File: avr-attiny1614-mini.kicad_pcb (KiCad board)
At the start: 2 copper layers, 0 parts

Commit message: Layout exploring
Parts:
- added C1: 100nF, local_footprints:0805_HS, F.Cu at (140.3, 138.4)
- added D1: D_Schottky, local_footprints:1206_Diode_HS, B.Cu at (149.9, 139.7)
- added J1: Conn_01x05, local_footprints:Pin_Header_Straight_1x05_Pitch2.54mm, F.Cu at (134.6, 144.8)
- added J10: UPDI, local_footprints:Pin_Header_Straight_1x01_Pitch2.54mm, F.Cu at (137.2, 134.6)
- added J2: Conn_01x06, local_footprints:Pin_Header_Straight_1x06_Pitch2.54mm, F.Cu at (139.7, 132.1)
- added J3: BAT_JST_PH, Connectors_JST:JST_PH_S2B-PH-K_02x2.00mm_Angled, F.Cu at (127.5, 142.2)
- added J4: GND, local_footprints:Pin_Header_Straight_1x01_Pitch2.54mm, F.Cu at (137.2, 132.1)
- added J5: GND, local_footprints:Pin_Header_Straight_1x01_Pitch2.54mm, F.Cu at (149.9, 144.8)
- added J6: VOUT1, local_footprints:Pin_Header_Straight_1x01_Pitch2.54mm, F.Cu at (152.4, 144.8)
- added J7: EXT_VIN, local_footprints:Pin_Header_Straight_1x01_Pitch2.54mm, F.Cu at (152.4, 135.9)
- added J8: EXT_LOAD+, local_footprints:Pin_Header_Straight_1x01_Pitch2.54mm, F.Cu at (152.4, 138.4)
- added J9: EXT_LOAD-, local_footprints:Pin_Header_Straight_1x01_Pitch2.54mm, F.Cu at (152.4, 141.0)
- added Q1: DMP2035U, local_footprints:SOT-23_HS, F.Cu at (130.8, 118.1)
- added Q2: NTR3C21NZ, local_footprints:SOT-23_HS, F.Cu at (156.2, 118.1)
- added R1: 3.3k, local_footprints:0805_HS, F.Cu at (137.2, 137.2)
- added R3: 100k, local_footprints:0805_HS, F.Cu at (135.9, 116.8)
- added R4: 100, local_footprints:1206_HS, F.Cu at (135.9, 119.4)
- added R5: 10k, local_footprints:0805_HS, F.Cu at (156.2, 125.7)
- added R6: 10k, local_footprints:0805_HS, F.Cu at (158.8, 125.7)
- added R7: 100, local_footprints:1206_HS, F.Cu at (130.8, 134.6)
- added R8: 1k, local_footprints:0805_HS, F.Cu at (151.1, 116.8)
- added R9: 100k, local_footprints:0805_HS, F.Cu at (151.1, 119.4)
- added SW1: SW_SPST, Buttons_Switches_THT:SW_PUSH_6mm, F.Cu at (133.3, 132.1)
- added U1: attiny1614, local_footprints:SOIC-14_3.9x8.7mm_Pitch1.27mm_HS, F.Cu at (146.1, 138.4)

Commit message: Approx placement for 1.2in x 0.6in board.
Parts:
- added J11: GND, local_footprints:Pin_Header_Straight_1x01_Pitch2.54mm, F.Cu at (127.0, 132.1)
- D1: moved to F.Cu
- Q1, R3, R4, R5, R6, R7: moved to B.Cu
- moved Q2 33.1 mm to (129.5, 137.7)
- moved R8 32.4 mm to (126.4, 137.8), turned to 90 degrees
- moved R9 32.4 mm to (124.5, 137.8), turned to 90 degrees
- moved J7 28.2 mm to (124.5, 132.1), turned to 90 degrees
- moved J8 23.7 mm to (129.5, 132.1), turned to 90 degrees
- moved J9 22.2 mm to (132.1, 132.1), turned to 90 degrees
- moved Q1 21.1 mm to (129.5, 139.2), turned to 0 degrees
- moved D1 20.9 mm to (129.5, 134.6), turned to 0 degrees
- moved R4 20.5 mm to (125.7, 137.2), turned to 270 degrees
- moved J6 20.3 mm to (132.1, 144.8)
- moved R3 19.5 mm to (129.4, 135.3)
- moved J4 13.0 mm to (134.6, 144.8)
- moved R5 11.8 mm to (149.9, 135.6)
- moved R6 11.8 mm to (152.4, 135.6), turned to 90 degrees
- moved R7 7.50 mm to (137.7, 137.7), turned to 90 degrees
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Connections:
- net Net-(D1-Pad1) renamed /EXT_VIN_LOAD+
- net Net-(D1-Pad2) renamed /EXT_LOAD-
- net Net-(J6-Pad1) renamed /VOUT1

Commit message: Routing part 1
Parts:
- removed the U1 at (148.6, 138.4)
- added U1 (x2): attiny1614, local_footprints:SOIC-14_3.9x8.7mm_Pitch1.27mm_HS, F.Cu at (148.6, 138.4)
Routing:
- net VIN: track 0.00 -> 20.5 mm, vias 0 -> 2
- net /~RESET: track 0.00 -> 18.9 mm, vias 0 -> 2
- net Net-(J1-Pad2): track 0.00 -> 8.36 mm
- net Net-(J1-Pad3): track 0.00 -> 8.20 mm
- net UPDI: track 0.00 -> 7.65 mm
- net /SCL: track 0.00 -> 6.84 mm
- net /SCK: track 0.00 -> 6.76 mm
- net Net-(R7-Pad1): track 0.00 -> 6.50 mm
- net /SDA: track 0.00 -> 6.34 mm
- net /RX: track 0.00 -> 6.33 mm
- net /TX: track 0.00 -> 5.38 mm
- net /MISO: track 0.00 -> 5.38 mm
- net GND: track 0.00 -> 5.38 mm
- net /MOSI: track 0.00 -> 4.43 mm

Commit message: Complete routing; Draft.
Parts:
- removed the U1 at (148.6, 138.4) (x2)
- added U1 (x2): attiny1614, local_footprints:SOIC-14_3.9x8.7mm_Pitch1.27mm_HS, F.Cu at (148.6, 138.4)
- moved J11 2.54 mm to (124.5, 132.1)
- moved J7 2.54 mm to (127.0, 132.1)
- moved R7 0.32 mm to (137.4, 137.7)
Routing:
- net GND: track 5.38 -> 39.2 mm, vias 0 -> 5
- net VEXT-EN: track 0.00 -> 28.6 mm, vias 0 -> 4
- net VOUT1-~EN: track 0.00 -> 24.9 mm, vias 0 -> 3
- net VIN: track 20.5 -> 43.4 mm, vias 2 -> 3
- net /VOUT1: track 0.00 -> 7.38 mm, vias 0 -> 2
- net /EXT_LOAD-: track 0.00 -> 7.15 mm
- net /EXT_VIN_LOAD+: track 0.00 -> 6.21 mm
- net Net-(Q1-Pad1): track 0.00 -> 4.93 mm, vias 0 -> 2
- net Net-(R7-Pad1): track 6.50 -> 9.70 mm
- net Net-(Q2-Pad1): track 0.00 -> 2.01 mm
- added copper zone on B.Cu, net GND
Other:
- board outline added: 30.5 x 15.2 mm

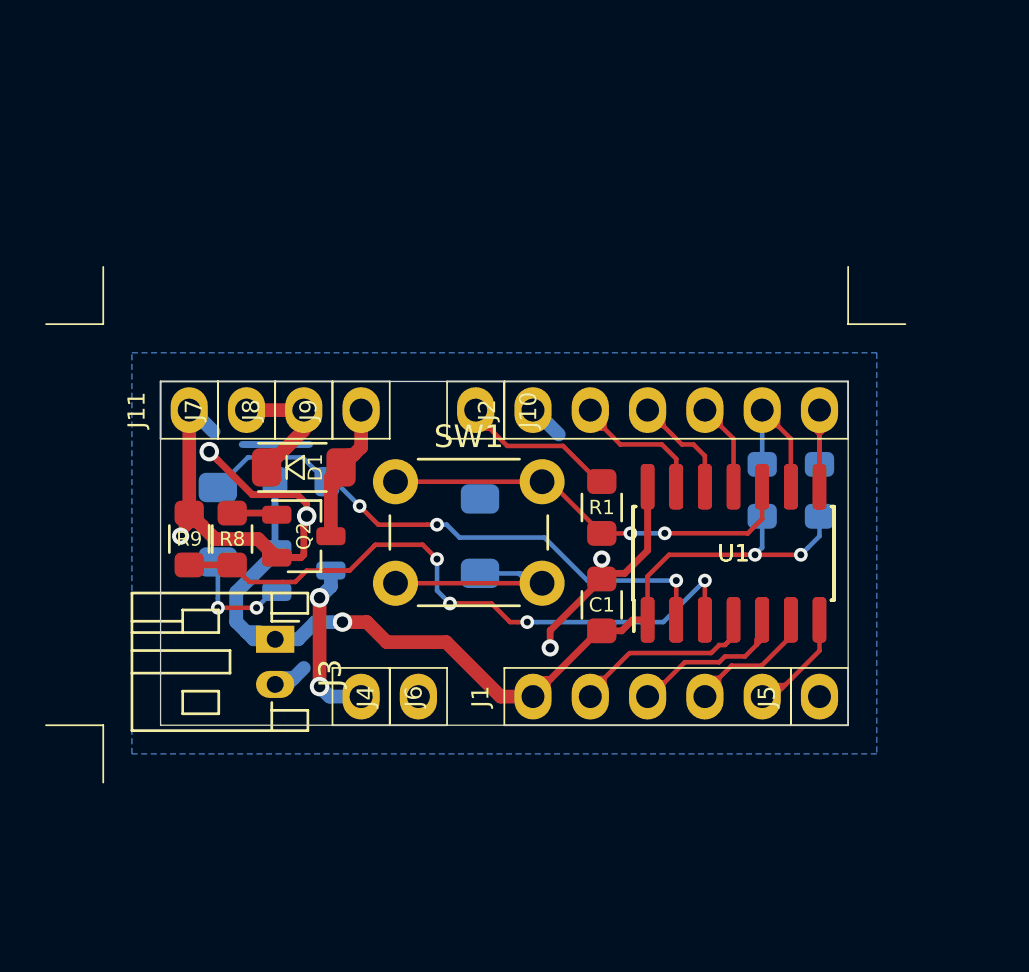
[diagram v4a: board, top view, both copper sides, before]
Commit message: Finished 1.2in x 0.6in layout
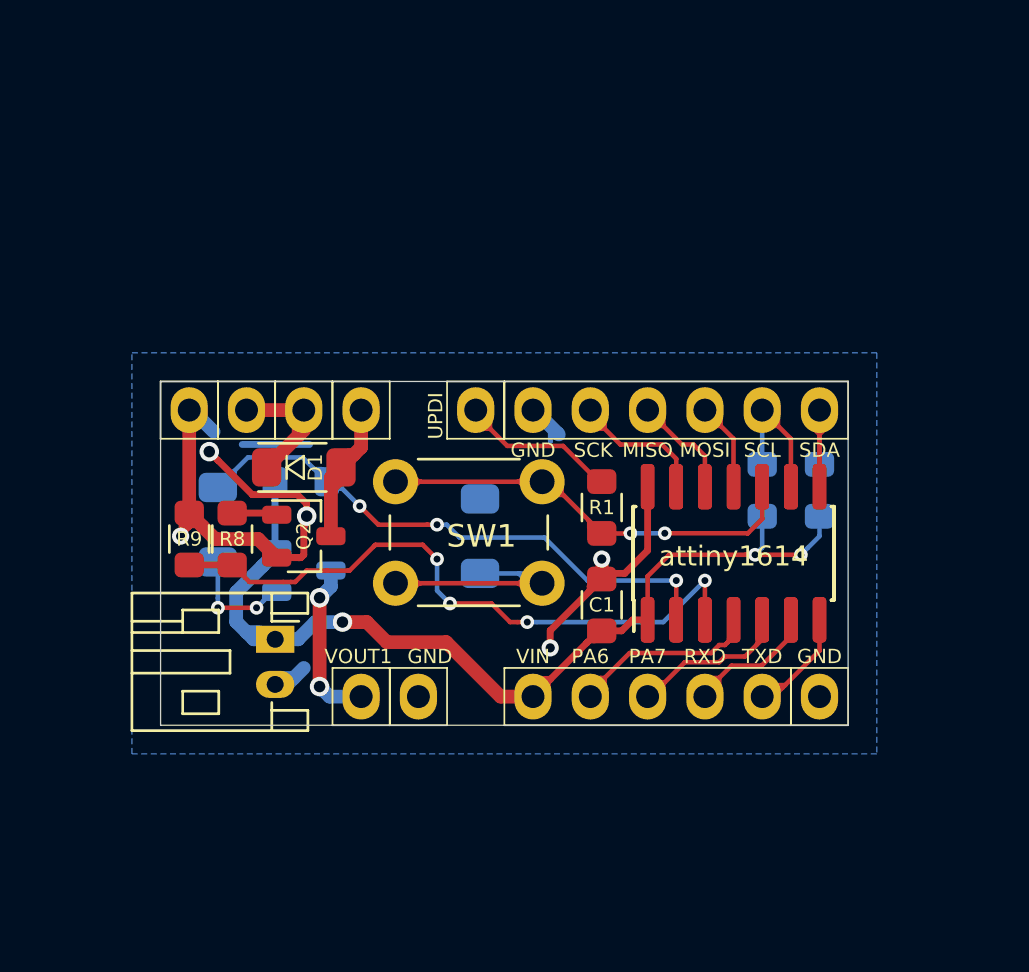
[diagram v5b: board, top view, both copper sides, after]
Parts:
- removed the U1 at (148.6, 138.4) (x2)
- added U1 (x2): attiny1614, local_footprints:SOIC-14_3.9x8.7mm_Pitch1.27mm_HS, F.Cu at (148.6, 138.4)
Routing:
- net /~RESET: track 18.9 -> 20.8 mm
- net GND: track 39.2 -> 40.9 mm
- net Net-(R7-Pad1): track 9.70 -> 10.9 mm
- net VIN: track 43.4 -> 44.4 mm
- net VOUT1-~EN: track 24.9 -> 25.8 mm
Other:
- board text added: "Belous"
- board text added: "CC BY-SA 4.0"
- board text added: "GND"
- board text added: "L+"
- board text added: "L-"
- board text added: "MISO"
- board text added: "MOSI"
- board text added: "PA1"
- board text added: "PA2"
- board text added: "PA3"
- board text added: "PA6"
- board text added: "PA7"
- board text added: "PB0"
- board text added: "PB1"
- board text added: "PB2"
- board text added: "PB3"
- board text added: "RXD"
- board text added: "SCK"
- board text added: "SCL"
- board text added: "SDA"
- board text added: "TXD"
- board text added: "UPDI"
- board text added: "VEXT"
- board text added: "VIN"
- board text added: "VOUT1"
- board text added: "Vlad"
- board text added: "attiny1614"
- board text added: "rev 1"
- board text added: "©"
